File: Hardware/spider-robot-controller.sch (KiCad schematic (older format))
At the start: 26 parts, among them CON1 AVR-ISP-6, CON2 BARREL_JACK, IC1 ATMEGA328-P, P1 SERVO_HEADER, P10 SERVO_HEADER, P11 SERVO_HEADER, P12 SERVO_HEADER, P13 Bluetooth_header, P2 SERVO_HEADER, P3 SERVO_HEADER, P4 SERVO_HEADER, P5 SERVO_HEADER, P6 SERVO_HEADER, P7 SERVO_HEADER, P8 SERVO_HEADER, P9 SERVO_HEADER, SW1 SW_PUSH, U1 LM7805, Y1 16MHz

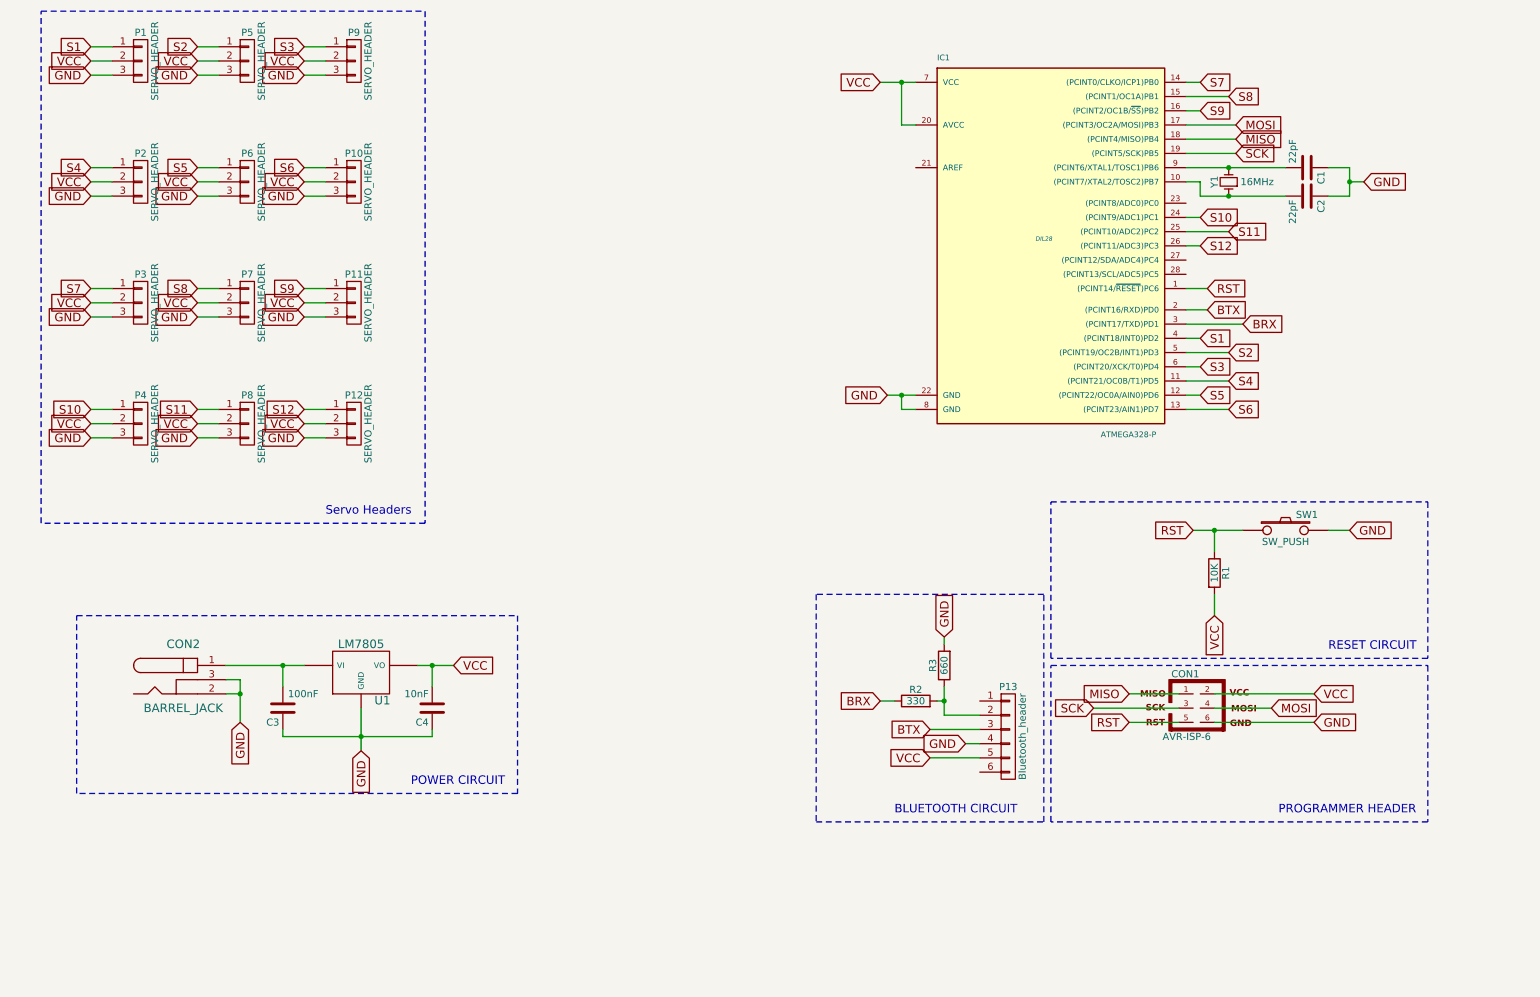
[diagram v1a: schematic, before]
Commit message: Improved power circuit - added switch
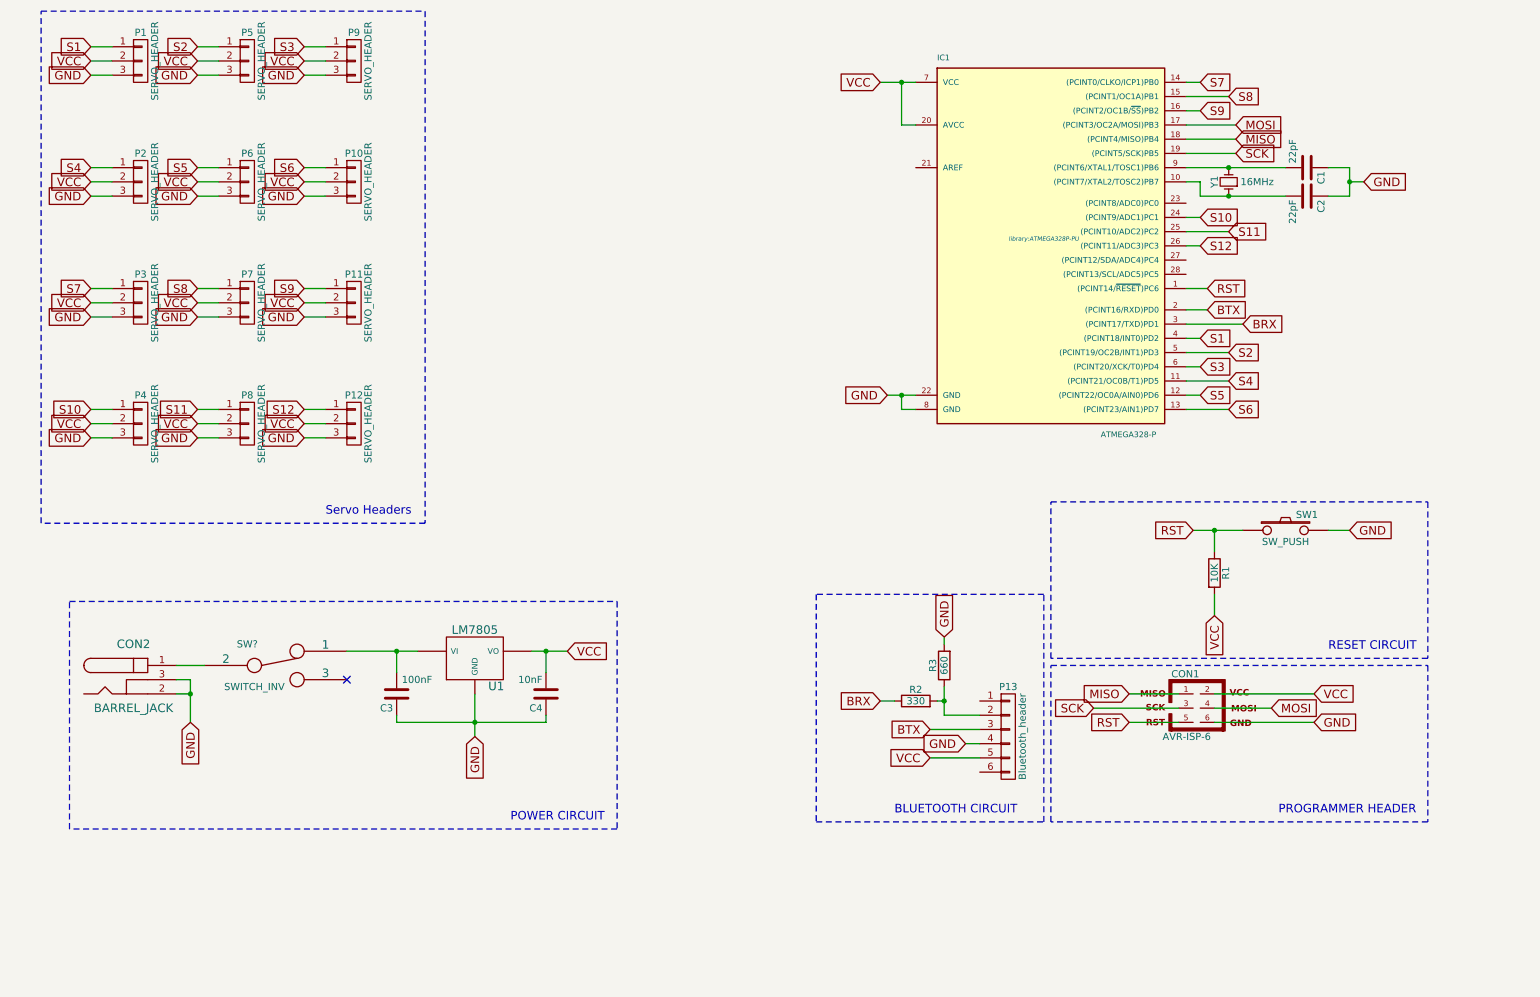
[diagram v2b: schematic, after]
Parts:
- added SW?: SWITCH_INV, symbol SWITCH_INV
- CON1: footprint AVR-ISP-6 -> Pin_Headers:Pin_Header_Straight_2x03
- IC1: footprint DIL28 -> library:ATMEGA328P-PU
- P1, P10, P11, P12, P2, P3, P4, P5, P6, P7, P8, P9: footprint Pin_Headers:Pin_Header_Angled_1x03 -> Pin_Headers:Pin_Header_Straight_1x03
- P13: footprint Pin_Headers:Pin_Header_Angled_1x06 -> Pin_Headers:Pin_Header_Straight_1x06
- SW1: footprint (none) -> library:SW_PUSH
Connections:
- net at C3.2, U1.VI: now also SW?.1; no longer CON2.1
- new net: CON2.1, SW?.2
- no-connect marks 0 -> 1
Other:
- moved on the sheet: C3, C4, CON2, U1
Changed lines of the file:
@@
 F 0 "CON1" H 8845 5690 50  0000 C CNN
 F 1 "AVR-ISP-6" H 8685 5220 50  0000 L BNN
-F 2 "AVR-ISP-6" V 8430 5490 50  0001 C CNN
+F 2 "Pin_Headers:Pin_Header_Straight_2x03" V 8430 5490 50  0001 C CNN
 F 3 "" H 8925 5450 60  0000 C CNN
 	1    8950 5450
@@
 F 0 "IC1" H 7100 3400 40  0000 L BNN
 F 1 "ATMEGA328-P" H 8250 750 40  0000 L BNN
-F 2 "DIL28" H 7850 2150 30  0000 C CIN
+F 2 "library:ATMEGA328P-PU" H 7850 2150 30  0000 C CIN
 F 3 "" H 7850 2150 60  0000 C CNN
 	1    7850 2150
@@
 F 0 "SW1" H 9700 4310 50  0000 C CNN
 F 1 "SW_PUSH" H 9550 4120 50  0000 C CNN
-F 2 "" H 9550 4200 60  0001 C CNN
+F 2 "library:SW_PUSH" H 9550 4200 60  0001 C CNN
 F 3 "" H 9550 4200 60  0000 C CNN
 	1    9550 4200
@@
 F 0 "P1" H 1500 1100 50  0000 C CNN
 F 1 "SERVO_HEADER" V 1600 900 50  0000 C CNN
-F 2 "Pin_Headers:Pin_Header_Angled_1x03" H 1500 900 60  0001 C CNN
+F 2 "Pin_Headers:Pin_Header_Straight_1x03" H 1500 900 60  0001 C CNN
 F 3 "" H 1500 900 60  0000 C CNN
 	1    1500 900
@@
 F 0 "P5" H 2250 1100 50  0000 C CNN
 F 1 "SERVO_HEADER" V 2350 900 50  0000 C CNN
-F 2 "Pin_Headers:Pin_Header_Angled_1x03" H 2250 900 60  0001 C CNN
+F 2 "Pin_Headers:Pin_Header_Straight_1x03" H 2250 900 60  0001 C CNN
 F 3 "" H 2250 900 60  0000 C CNN
 	1    2250 900
@@
 F 0 "P9" H 3000 1100 50  0000 C CNN
 F 1 "SERVO_HEADER" V 3100 900 50  0000 C CNN
-F 2 "Pin_Headers:Pin_Header_Angled_1x03" H 3000 900 60  0001 C CNN
+F 2 "Pin_Headers:Pin_Header_Straight_1x03" H 3000 900 60  0001 C CNN
 F 3 "" H 3000 900 60  0000 C CNN
 	1    3000 900
@@
 F 0 "P2" H 1500 1950 50  0000 C CNN
 F 1 "SERVO_HEADER" V 1600 1750 50  0000 C CNN
-F 2 "Pin_Headers:Pin_Header_Angled_1x03" H 1500 1750 60  0001 C CNN
+F 2 "Pin_Headers:Pin_Header_Straight_1x03" H 1500 1750 60  0001 C CNN
 F 3 "" H 1500 1750 60  0000 C CNN
 	1    1500 1750
@@
 F 0 "P6" H 2250 1950 50  0000 C CNN
 F 1 "SERVO_HEADER" V 2350 1750 50  0000 C CNN
-F 2 "Pin_Headers:Pin_Header_Angled_1x03" H 2250 1750 60  0001 C CNN
+F 2 "Pin_Headers:Pin_Header_Straight_1x03" H 2250 1750 60  0001 C CNN
 F 3 "" H 2250 1750 60  0000 C CNN
 	1    2250 1750
@@
 F 0 "P10" H 3000 1950 50  0000 C CNN
 F 1 "SERVO_HEADER" V 3100 1750 50  0000 C CNN
-F 2 "Pin_Headers:Pin_Header_Angled_1x03" H 3000 1750 60  0001 C CNN
+F 2 "Pin_Headers:Pin_Header_Straight_1x03" H 3000 1750 60  0001 C CNN
 F 3 "" H 3000 1750 60  0000 C CNN
 	1    3000 1750
@@
 F 0 "P3" H 1500 2800 50  0000 C CNN
 F 1 "SERVO_HEADER" V 1600 2600 50  0000 C CNN
-F 2 "Pin_Headers:Pin_Header_Angled_1x03" H 1500 2600 60  0001 C CNN
+F 2 "Pin_Headers:Pin_Header_Straight_1x03" H 1500 2600 60  0001 C CNN
 F 3 "" H 1500 2600 60  0000 C CNN
 	1    1500 2600
@@
 F 0 "P7" H 2250 2800 50  0000 C CNN
 F 1 "SERVO_HEADER" V 2350 2600 50  0000 C CNN
-F 2 "Pin_Headers:Pin_Header_Angled_1x03" H 2250 2600 60  0001 C CNN
+F 2 "Pin_Headers:Pin_Header_Straight_1x03" H 2250 2600 60  0001 C CNN
 F 3 "" H 2250 2600 60  0000 C CNN
 	1    2250 2600
@@
 F 0 "P11" H 3000 2800 50  0000 C CNN
 F 1 "SERVO_HEADER" V 3100 2600 50  0000 C CNN
-F 2 "Pin_Headers:Pin_Header_Angled_1x03" H 3000 2600 60  0001 C CNN
+F 2 "Pin_Headers:Pin_Header_Straight_1x03" H 3000 2600 60  0001 C CNN
 F 3 "" H 3000 2600 60  0000 C CNN
 	1    3000 2600
@@
 F 0 "P4" H 1500 3650 50  0000 C CNN
 F 1 "SERVO_HEADER" V 1600 3450 50  0000 C CNN
-F 2 "Pin_Headers:Pin_Header_Angled_1x03" H 1500 3450 60  0001 C CNN
+F 2 "Pin_Headers:Pin_Header_Straight_1x03" H 1500 3450 60  0001 C CNN
 F 3 "" H 1500 3450 60  0000 C CNN
 	1    1500 3450
@@
 F 0 "P8" H 2250 3650 50  0000 C CNN
 F 1 "SERVO_HEADER" V 2350 3450 50  0000 C CNN
-F 2 "Pin_Headers:Pin_Header_Angled_1x03" H 2250 3450 60  0001 C CNN
+F 2 "Pin_Headers:Pin_Header_Straight_1x03" H 2250 3450 60  0001 C CNN
 F 3 "" H 2250 3450 60  0000 C CNN
 	1    2250 3450
@@
 F 0 "P12" H 3000 3650 50  0000 C CNN
 F 1 "SERVO_HEADER" V 3100 3450 50  0000 C CNN
-F 2 "Pin_Headers:Pin_Header_Angled_1x03" H 3000 3450 60  0001 C CNN
+F 2 "Pin_Headers:Pin_Header_Straight_1x03" H 3000 3450 60  0001 C CNN
 F 3 "" H 3000 3450 60  0000 C CNN
 	1    3000 3450
@@
 L BARREL_JACK CON2
 U 1 1 55F99D4A
-P 1800 5250
-F 0 "CON2" H 1800 5500 60  0000 C CNN
-F 1 "BARREL_JACK" H 1800 5050 60  0000 C CNN
-F 2 "library:BARREL_JACK" H 1800 5250 60  0001 C CNN
-F 3 "" H 1800 5250 60  0000 C CNN
-	1    1800 5250
+P 1450 5250
+F 0 "CON2" H 1450 5500 60  0000 C CNN
+F 1 "BARREL_JACK" H 1450 5050 60  0000 C CNN
+F 2 "library:BARREL_JACK" H 1450 5250 60  0001 C CNN
+F 3 "" H 1450 5250 60  0000 C CNN
+	1    1450 5250
 	1    0    0    -1
 $EndComp
@@
 L LM7805 U1
 U 1 1 55F99DFD
-P 3050 5200
-F 0 "U1" H 3200 5004 60  0000 C CNN
-F 1 "LM7805" H 3050 5400 60  0000 C CNN
-F 2 "library:LM7805" H 3050 5200 60  0001 C CNN
-F 3 "" H 3050 5200 60  0000 C CNN
-	1    3050 5200
-	1    0    0    -1
-$EndComp
-Wire Wire Line
-	2100 5150 2650 5150
-Wire Wire Line
-	2100 5250 2200 5250
-Wire Wire Line
-	2200 5350 2100 5350
-Text GLabel 3700 5150 2    60   Input ~ 0
+P 3850 5100
+F 0 "U1" H 4000 4904 60  0000 C CNN
+F 1 "LM7805" H 3850 5300 60  0000 C CNN
+F 2 "library:LM7805" H 3850 5100 60  0001 C CNN
+F 3 "" H 3850 5100 60  0000 C CNN
+	1    3850 5100
+	1    0    0    -1
+$EndComp
+Wire Wire Line
+	1750 5250 1850 5250
+Wire Wire Line
+	1850 5350 1750 5350
+Text GLabel 4500 5050 2    60   Input ~ 0
 VCC
 $Comp
 L C C3
 U 1 1 55F9A6BA
-P 2500 5450
-F 0 "C3" H 2525 5550 50  0000 L CNN
-F 1 "100nF" H 2250 5350 50  0000 L CNN
-F 2 "Capacitors_ThroughHole:C_Radial_D10_L13_P5" H 2538 5300 30  0001 C CNN
-F 3 "" H 2500 5450 60  0000 C CNN
-	1    2500 5450
+P 3300 5350
+F 0 "C3" H 3325 5450 50  0000 L CNN
+F 1 "100nF" H 3050 5250 50  0000 L CNN
+F 2 "Capacitors_ThroughHole:C_Radial_D10_L13_P5" H 3338 5200 30  0001 C CNN
+F 3 "" H 3300 5350 60  0000 C CNN
+	1    3300 5350
 	-1   0    0    1
 $EndComp
-Connection ~ 2500 5150
-Wire Wire Line
-	2500 5150 2500 5300
+Connection ~ 3300 5050
+Wire Wire Line
+	3300 5050 3300 5200
 $Comp
 L C C4
 U 1 1 55F9AD53
-P 3550 5450
-F 0 "C4" H 3575 5550 50  0000 L CNN
-F 1 "10nF" H 3575 5350 50  0000 L CNN
-F 2 "Capacitors_ThroughHole:C_Radial_D5_L6_P2.5" H 3588 5300 30  0001 C CNN
-F 3 "" H 3550 5450 60  0000 C CNN
-	1    3550 5450
+P 4350 5350
+F 0 "C4" H 4375 5450 50  0000 L CNN
+F 1 "10nF" H 4375 5250 50  0000 L CNN
+F 2 "Capacitors_ThroughHole:C_Radial_D5_L6_P2.5" H 4388 5200 30  0001 C CNN
+F 3 "" H 4350 5350 60  0000 C CNN
+	1    4350 5350
 	-1   0    0    1
 $EndComp
 Wire Wire Line
-	3450 5150 3700 5150
-Connection ~ 3550 5150
-Wire Wire Line
-	3550 5300 3550 5150
-Wire Wire Line
-	2200 5250 2200 5550
-Connection ~ 2200 5350
-Text GLabel 2200 5550 3    60   Input ~ 0
-GND
-Text GLabel 3050 5750 3    60   Input ~ 0
-GND
-Wire Wire Line
-	3050 5450 3050 5750
-Wire Wire Line
-	2500 5600 2500 5650
-Wire Wire Line
-	2500 5650 3550 5650
-Connection ~ 3050 5650
-Wire Wire Line
-	3550 5650 3550 5600
+	4250 5050 4500 5050
+Connection ~ 4350 5050
+Wire Wire Line
+	4350 5200 4350 5050
+Wire Wire Line
+	1850 5250 1850 5550
+Connection ~ 1850 5350
+Text GLabel 1850 5550 3    60   Input ~ 0
+GND
+Text GLabel 3850 5650 3    60   Input ~ 0
+GND
+Wire Wire Line
+	3850 5350 3850 5650
+Wire Wire Line
+	3300 5500 3300 5550
+Wire Wire Line
+	3300 5550 4350 5550
+Connection ~ 3850 5550
+Wire Wire Line
+	4350 5550 4350 5500
 $Comp
 L CONN_01X06 P13
@@
 F 0 "P13" H 7600 6000 50  0000 C CNN
 F 1 "Bluetooth_header" V 7700 5650 50  0000 C CNN
-F 2 "Pin_Headers:Pin_Header_Angled_1x06" H 7600 5650 60  0001 C CNN
+F 2 "Pin_Headers:Pin_Header_Straight_1x06" H 7600 5650 60  0001 C CNN
 F 3 "" H 7600 5650 60  0000 C CNN
 	1    7600 5650
@@
 Text Notes 6800 6200 0    60   ~ 0
 BLUETOOTH CIRCUIT
-Wire Notes Line
-	4150 6050 1050 6050
-Wire Notes Line
-	1050 6050 1050 4800
-Wire Notes Line
-	1050 4800 4150 4800
-Wire Notes Line
-	4150 4800 4150 6050
-Text Notes 3400 6000 0    60   ~ 0
+Text Notes 4100 6250 0    60   ~ 0
 POWER CIRCUIT
+$Comp
+L SWITCH_INV SW?
+U 1 1 55FA1051
+P 2450 5150
+F 0 "SW?" H 2250 5300 50  0000 C CNN
+F 1 "SWITCH_INV" H 2300 5000 50  0000 C CNN
+F 2 "" H 2450 5150 60  0000 C CNN
+F 3 "" H 2450 5150 60  0000 C CNN
+	1    2450 5150
+	1    0    0    -1
+$EndComp
+Wire Wire Line
+	1950 5150 1750 5150
+Wire Wire Line
+	2950 5050 3450 5050
+NoConn ~ 2950 5250
+Wire Notes Line
+	1000 4700 4850 4700
+Wire Notes Line
+	4850 4700 4850 6300
+Wire Notes Line
+	4850 6300 1000 6300
+Wire Notes Line
+	1000 6300 1000 4700
 $EndSCHEMATC

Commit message: working on pcb
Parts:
- added D1: LED, LEDs:LED-5MM, symbol LED
- added P14, P15, P16, P17, P18, P19, P20, P21, P? (x2): CONN_01X01, Pin_Headers:Pin_Header_Straight_1x01, symbol CONN_01X01
- added R4: 330, Resistors_ThroughHole:Resistor_Horizontal_RM10mm, symbol R
- SW2: renamed from SW?; footprint (none) -> library:SWITCH_INVERTER
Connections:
- net BRX: now also P14.1 (P1), P16.1 (P1)
- net GND: now also P19.1 (P1), P21.1 (P1), P?.1 (P1), P?.1 (P1), R4.1
- net RST: now also P18.1 (P1), P20.1 (P1)
- net SCK: now also P15.1 (P1), P17.1 (P1)
- net VCC: now also D1.2 (A)
- new net: D1.1 (K), R4.2
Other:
- moved on the sheet: C1, C2, C3, C4, CON2, IC1, P1, P10, P11, P12, P2, P3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

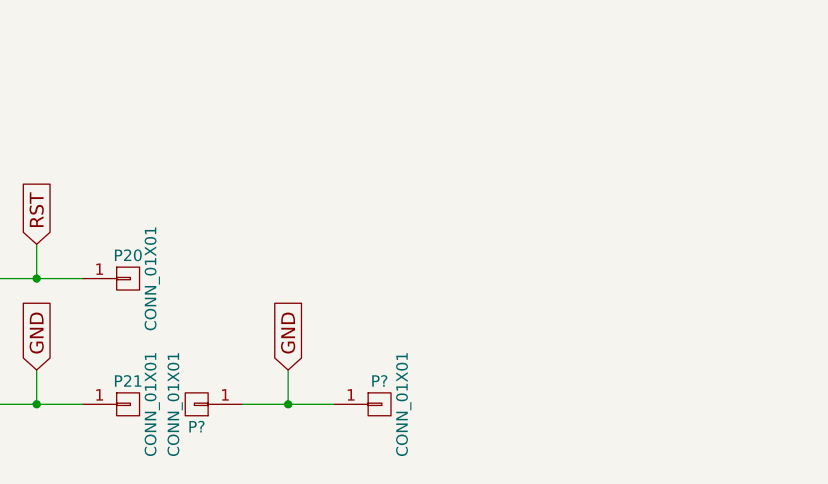
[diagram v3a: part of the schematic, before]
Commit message: improved pcb layout traces
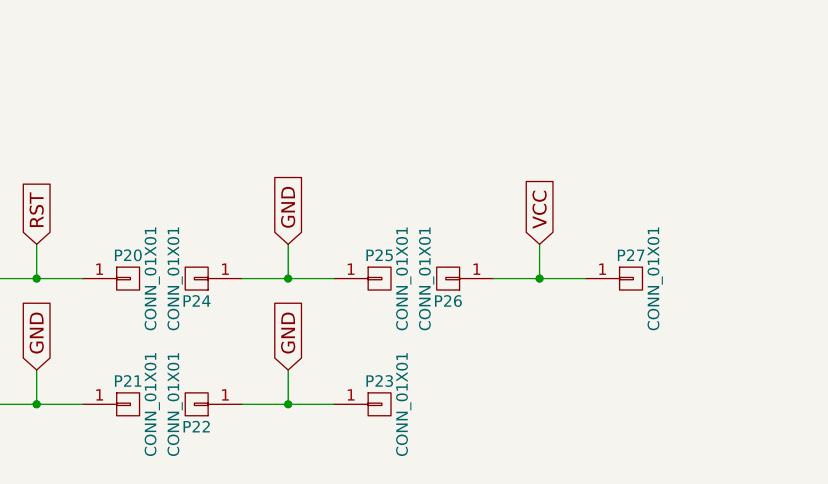
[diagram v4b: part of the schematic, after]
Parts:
- added P24, P25, P26, P27: CONN_01X01, Pin_Headers:Pin_Header_Straight_1x01, symbol CONN_01X01
- gave numbers to parts that had none: 2
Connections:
- net GND: now also P24.1 (P1), P25.1 (P1)
- net VCC: now also P26.1 (P1), P27.1 (P1)
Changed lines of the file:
@@
 LIBS:contrib
 LIBS:valves
-LIBS:arduino_shieldsNCL
 LIBS:Header1x01
 LIBS:spider-robot-controller-cache
@@
 GND
 $Comp
-L CONN_01X01 P?
+L CONN_01X01 P23
 U 1 1 55FA6089
 P 4000 7000
-F 0 "P?" H 4000 7100 50  0000 C CNN
+F 0 "P23" H 4000 7100 50  0000 C CNN
 F 1 "CONN_01X01" V 4100 7000 50  0000 C CNN
 F 2 "Pin_Headers:Pin_Header_Straight_1x01" H 4000 7000 60  0001 C CNN
@@
 $EndComp
 $Comp
-L CONN_01X01 P?
+L CONN_01X01 P22
 U 1 1 55FA608F
 P 3200 7000
-F 0 "P?" H 3200 7100 50  0000 C CNN
+F 0 "P22" H 3200 7100 50  0000 C CNN
 F 1 "CONN_01X01" V 3300 7000 50  0000 C CNN
 F 2 "Pin_Headers:Pin_Header_Straight_1x01" H 3200 7000 60  0001 C CNN
@@
 Text GLabel 3600 6850 1    60   Input ~ 0
 GND
+$Comp
+L CONN_01X01 P25
+U 1 1 55FA711C
+P 4000 6450
+F 0 "P25" H 4000 6550 50  0000 C CNN
+F 1 "CONN_01X01" V 4100 6450 50  0000 C CNN
+F 2 "Pin_Headers:Pin_Header_Straight_1x01" H 4000 6450 60  0001 C CNN
+F 3 "" H 4000 6450 60  0000 C CNN
+	1    4000 6450
+	1    0    0    -1
+$EndComp
+$Comp
+L CONN_01X01 P24
+U 1 1 55FA7122
+P 3200 6450
+F 0 "P24" H 3200 6550 50  0000 C CNN
+F 1 "CONN_01X01" V 3300 6450 50  0000 C CNN
+F 2 "Pin_Headers:Pin_Header_Straight_1x01" H 3200 6450 60  0001 C CNN
+F 3 "" H 3200 6450 60  0000 C CNN
+	1    3200 6450
+	-1   0    0    1
+$EndComp
+Wire Wire Line
+	3400 6450 3800 6450
+Wire Wire Line
+	3600 6450 3600 6300
+Connection ~ 3600 6450
+Text GLabel 3600 6300 1    60   Input ~ 0
+GND
+$Comp
+L CONN_01X01 P27
+U 1 1 55FA786D
+P 5100 6450
+F 0 "P27" H 5100 6550 50  0000 C CNN
+F 1 "CONN_01X01" V 5200 6450 50  0000 C CNN
+F 2 "Pin_Headers:Pin_Header_Straight_1x01" H 5100 6450 60  0001 C CNN
+F 3 "" H 5100 6450 60  0000 C CNN
+	1    5100 6450
+	1    0    0    -1
+$EndComp
+$Comp
+L CONN_01X01 P26
+U 1 1 55FA7873
+P 4300 6450
+F 0 "P26" H 4300 6550 50  0000 C CNN
+F 1 "CONN_01X01" V 4400 6450 50  0000 C CNN
+F 2 "Pin_Headers:Pin_Header_Straight_1x01" H 4300 6450 60  0001 C CNN
+F 3 "" H 4300 6450 60  0000 C CNN
+	1    4300 6450
+	-1   0    0    1
+$EndComp
+Wire Wire Line
+	4500 6450 4900 6450
+Wire Wire Line
+	4700 6450 4700 6300
+Connection ~ 4700 6450
+Text GLabel 4700 6300 1    60   Input ~ 0
+VCC
 $EndSCHEMATC
